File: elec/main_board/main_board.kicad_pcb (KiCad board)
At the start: 2 copper layers, 80 x 80 mm, 163 parts, among them J10 MJ-179PH, J13 B6B-ZR, J14 PinHeader, J15 PinHeader, J16 Fan motor, J2 Conn_01x22_Female, J3 PinHeader, J4 Conn_01x02, J5 Conn_01x02, J6 B6B-ZR, J7 EncSide, J8 B6B-ZR, J9 EncSide, Q1 DTC114E, Q10 IRLML6344, Q11 DMT6008LFG, Q12 DMT6008LFG, Q13 DMT6008LFG, Q14 MMBT3904, Q2 DTC114E, Q3 ST-1KL3A, Q4 ST-1KL3A, Q5 ST-1KL3A, Q6 ST-1KL3A, Q7 IRLML6344, Q8 IRLML6344, Q9 IRLML6344, SW1 TS-1088-AR02016, SW2 TS-1088-AR02016, SW3 TS-1088-AR02016, SW4 TS-1088-AR02016, SW5 TS-1088-AR02016, SW6 TS-1088-AR02016, U1 74LVC1G07SE-7, U10 LSM6DSR, U11 OKL-T/6-W12N-C, U12 XC6221B332MR, U13 LM74700QDBVRQ1, U14 MCP73213T-A6SI/MF, U15 LM74700QDBVRQ1, U16 FT231XQ-R, U17 FT231XQ-R, U18 SL2.1A, U19 INA219AIDCN, U2 ADCS7476, U20 ATmega328P-AU, U22 ESP32-S3-FN8, U3 ADCS7476, U4 BD63573NUV, U5 BD63573NUV, U6 ADCS7476, U7 ADCS7476, U8 AS5047D, U9 AS5047D, X1 CSTCE16M0V53-R0, X2 830108208709, Y2 X322512MSB4SI

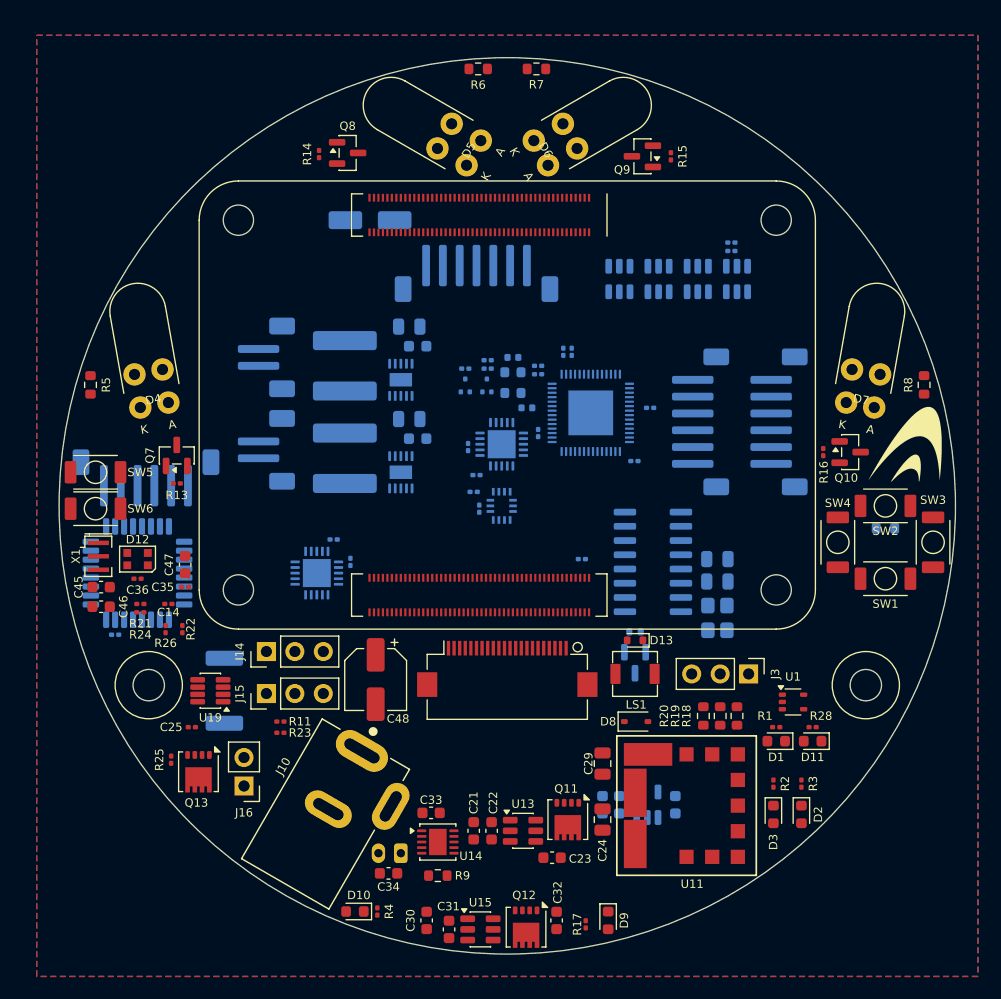
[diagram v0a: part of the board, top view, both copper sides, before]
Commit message: 配線作業中
Signed-off-by: Kazuki Iida <elkel53930@gmail.com>
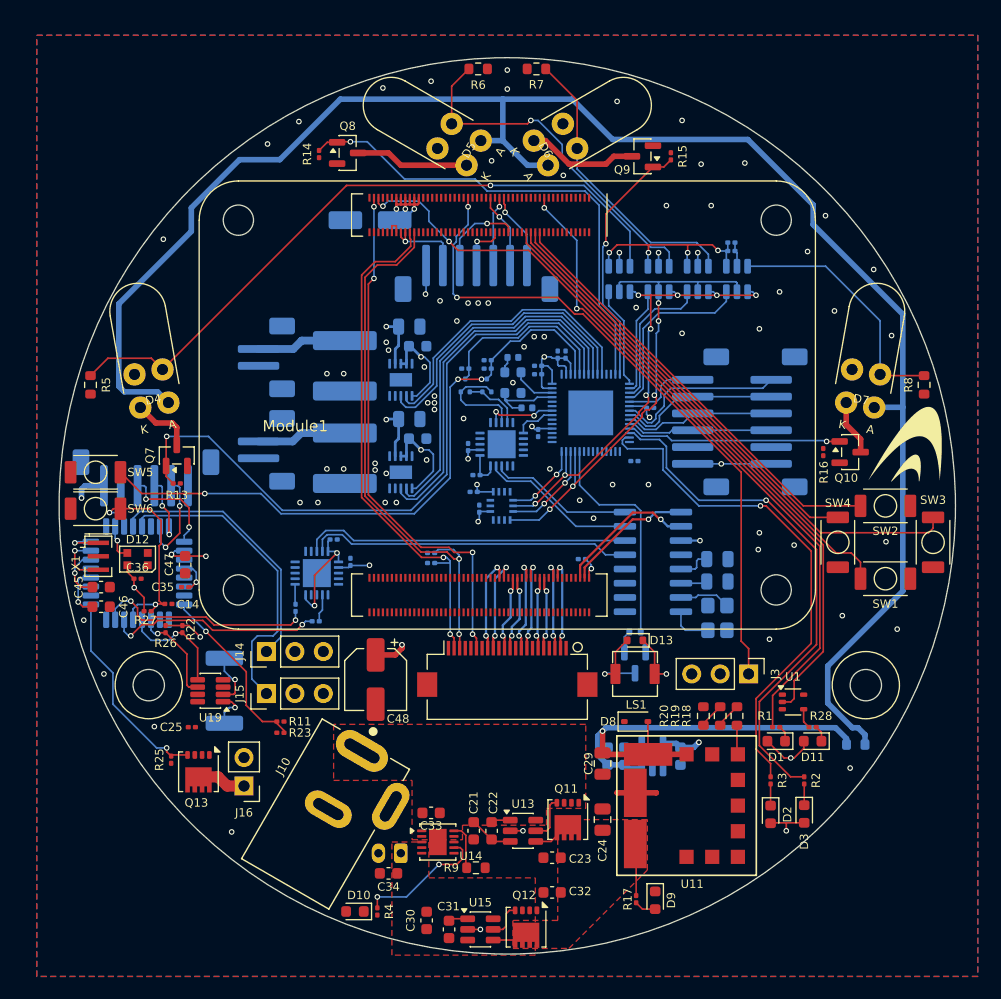
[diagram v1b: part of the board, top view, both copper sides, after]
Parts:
- added R32: RC0201FR-071KL, Resistor_SMD:R_0201_0603Metric, B.Cu at (138.2, 99.2)
- added R33: RC0201FR-071KL, Resistor_SMD:R_0201_0603Metric, B.Cu at (138.2, 100.1)
- R21, R24: moved to B.Cu
- R27: moved to F.Cu
- moved R12 19.5 mm to (176.1, 116.3)
- moved R24 15.7 mm to (127.9, 105.3), turned to 0 degrees
- moved R21 13.9 mm to (126.1, 104.1), turned to -90 degrees
- moved R17 5.03 mm to (156.5, 130.1)
- moved D9 4.57 mm to (158.2, 130.2)
- moved C26 4.36 mm to (153.9, 117.3)
- moved C27 4.36 mm to (155.4, 117.3)
- moved C28 4.36 mm to (160.4, 117.3)
- moved U12 4.36 mm to (157.9, 117.3)
- moved R27 3.58 mm to (112.9, 104.4)
- moved R9 3.47 mm to (142.2, 127.3), turned to 180 degrees
- moved R2 2.76 mm to (171.5, 119.5)
- moved R3 2.76 mm to (168.5, 119.5)
- moved D3 2.75 mm to (171.5, 122.5)
- moved D2 2.75 mm to (168.5, 122.5)
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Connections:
- C36 pad 1: GND -> +5V
- C36 pad 2: +5V -> GND
- J1 pad 2: /Compute Module/CM3V3 -> +3V3CM
- Module1 pad 24: unconnected-(Module1A-GPIO26-Pad24) -> /Compute Module/BTN_UP
- Module1 pad 26: unconnected-(Module1A-GPIO19-Pad26) -> /Compute Module/BTN_LEFT
- Module1 pad 28: unconnected-(Module1A-GPIO13-Pad28) -> /Compute Module/BTN_RIGHT
- Module1 pad 30: unconnected-(Module1A-GPIO6-Pad30) -> /Compute Module/BTN_DOWN
- Module1 pad 50: /Compute Module/BTN_RIGHT -> unconnected-(Module1A-GPIO17-Pad50)
- Module1 pad 54: /Compute Module/BTN_LEFT -> unconnected-(Module1A-GPIO4-Pad54)
- Module1 pad 56: /Compute Module/BTN_UP -> unconnected-(Module1A-GPIO3-Pad56)
- Module1 pad 58: /Compute Module/BTN_DOWN -> unconnected-(Module1A-GPIO2-Pad58)
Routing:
- net +3V3: track 0.00 -> 281.1 mm, vias 0 -> 16
- net +5V: track 0.00 -> 266.7 mm, vias 0 -> 15
- net Net-(D4-A): track 0.00 -> 156.2 mm
- net /Compute Module/nPWR_LED: track 0.00 -> 69.7 mm, vias 0 -> 2
- net Net-(Q3-E): track 0.00 -> 60.8 mm, vias 0 -> 1
- net /Micromouse/LF_EN: track 0.00 -> 60.4 mm, vias 0 -> 1
- net /Compute Module/FSV_SIG: track 0.00 -> 59.7 mm, vias 0 -> 2
- net Net-(Module1A-PI_nLED_Activity): track 0.00 -> 59.5 mm, vias 0 -> 2
- net /Micromouse/CHIP_PU: track 0.00 -> 57.3 mm, vias 0 -> 3
- net /Compute Module/BTN_RIGHT: track 0.00 -> 48.7 mm
- net /Compute Module/SCL0: track 0.00 -> 47.9 mm, vias 0 -> 2
- net /Micromouse/LED_1: track 0.00 -> 46.9 mm, vias 0 -> 1
- net /Compute Module/CAM_GPIO: track 0.00 -> 46.8 mm, vias 0 -> 4
- net /Compute Module/SDA0: track 0.00 -> 46.1 mm, vias 0 -> 2
- net /Micromouse/LED_0: track 0.00 -> 45.7 mm, vias 0 -> 1
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- added copper zone on F.Cu, net +BATT
- added copper zone on F.Cu, net /Power/EXT_PWR
- added copper zone on In1.Cu, net GND
- added copper zone on F.Cu, net Net-(BT1-+)
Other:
- copper layers 2 -> 4

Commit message: アートワーク完了
Signed-off-by: Kazuki Iida <elkel53930@gmail.com>
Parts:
- removed H1, H2, H3, H4: M2 mounting hole, MountingHole:MountingHole_2.2mm_M2
- removed J15: PinHeader, Connector_PinHeader_2.54mm:PinHeader_1x03_P2.54mm_Vertical
- removed U8, U9: AS5047D, Package_SO:TSSOP-14_4.4x5mm_P0.65mm
- added Q15: IRLML6344, Package_TO_SOT_SMD:SOT-23, B.Cu at (123.7, 108.8)
- added Q16: IRLML6344, Package_TO_SOT_SMD:SOT-23, B.Cu at (158.4, 68.0)
- added R34: 0603WAF1001T5E, Resistor_SMD:R_0603_1608Metric, B.Cu at (125.0, 113.6)
- added R35: RC0201FR-0710KL, Resistor_SMD:R_0201_0603Metric, B.Cu at (123.7, 106.5)
- added R36: 0603WAF1001T5E, Resistor_SMD:R_0603_1608Metric, B.Cu at (122.6, 112.4)
- added R37: RC0201FR-0710KL, Resistor_SMD:R_0201_0603Metric, B.Cu at (155.6, 67.8)
- C17: value CC0603KRX7R9BB104 -> CL10A475KO8NNNC; footprint Capacitor_SMD:C_0402_1005Metric -> Capacitor_SMD:C_0603_1608Metric; moved to B.Cu
- C18: value CL05B104KO5NNNC -> CL32A107MPVNNNE; footprint Capacitor_SMD:C_0402_1005Metric -> Capacitor_SMD:C_1210_3225Metric; moved to B.Cu
- C48: value RVT1A101M0505 -> CL32A107MPVNNNE; footprint Capacitor_SMD:CP_Elec_5x5.4 -> Capacitor_SMD:C_1210_3225Metric; moved to B.Cu
- C49: value RVT1A101M0505 -> CL32A107MPVNNNE; footprint Capacitor_SMD:CP_Elec_5x5.4 -> Capacitor_SMD:C_1210_3225Metric
- J7: value EncSide -> B4B-ZR; footprint Library:EncoderPad -> Connector_JST:JST_ZH_B4B-ZR_1x04_P1.50mm_Vertical
- J9: value EncSide -> B2B-ZR; footprint Library:EncoderPad -> Connector_JST:JST_ZH_B2B-ZR_1x02_P1.50mm_Vertical
- moved C17 181.1 mm to (137.4, 106.2), turned to 180 degrees
- moved J7 172.1 mm to (129.4, 111.0), turned to 180 degrees
- moved J9 164.3 mm to (165.2, 64.2), turned to 180 degrees
- moved C18 151.0 mm to (135.1, 70.9), turned to 90 degrees
- moved C49 50.5 mm to (124.7, 119.3), turned to 90 degrees
- moved R12 15.2 mm to (161.7, 121.0)
- moved J14 10.4 mm to (133.8, 107.9), turned to 0 degrees
- moved C48 6.12 mm to (132.8, 104.4)
- moved C25 6.08 mm to (119.1, 109.1)
- moved C26 1.56 mm to (153.9, 118.9), turned to 90 degrees
- moved C27 1.56 mm to (155.4, 118.9), turned to 90 degrees
- moved R23 1.00 mm to (124.1, 116.0), turned to 0 degrees
- moved R11 0.99 mm to (124.1, 115.0)
- moved SW5 0.99 mm to (109.1, 91.5)
- moved R6 0.90 mm to (142.4, 56.9)
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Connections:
- C17 pad 1: Net-(J7-Pin_2) -> +3V3CM
- C17 pad 2: Net-(J7-Pin_1) -> GND
- C18 pad 1: Net-(J9-Pin_2) -> GND
- C18 pad 2: Net-(J9-Pin_1) -> +5V
- C48 pad 1: +5V -> GND
- C48 pad 2: GND -> +5V
- C49 pad 1: +5V -> GND
- C49 pad 2: GND -> +BATT
- J7 pad 1: Net-(J7-Pin_1) -> +5V
- J7 pad 3: Net-(J7-Pin_3) -> +5V
- J7 pad 4: Net-(J7-Pin_4) -> /Arm/BD_AD
- J9 pad 1: Net-(J9-Pin_1) -> +BATT
- Module1 pad 25: unconnected-(Module1A-GPIO21-Pad25) -> /Compute Module/LIGHT
- U20 pad 13: /Arm/SERVO_SIG2 -> /Arm/BD_EN
- U20 pad 23: unconnected-(U20-PC0-Pad23) -> /Arm/BD_AD
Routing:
- net +3V3CM: track 7.22 -> 50.6 mm, vias 1 -> 6
- net /Arm/SERVO_SIG2: track 28.2 -> 0.00 mm
- net /Arm/BD_EN: track 0.00 -> 22.8 mm
- net +3V3: track 281.1 -> 298.6 mm, vias 16 -> 19
- net Net-(U17-~{DTR}): track 0.00 -> 15.9 mm, vias 0 -> 1
- net /Arm/BD_AD: track 0.00 -> 15.8 mm
- net /Power/EXT_PWR: track 3.98 -> 18.9 mm
- net /Compute Module/LIGHT: track 0.00 -> 11.7 mm, vias 0 -> 1
- net Net-(U16-3V3OUT): track 3.35 -> 11.6 mm, vias 0 -> 2
- net /Arm/SERVO_SIG1: track 24.2 -> 31.7 mm
- net GND: track 20.3 -> 27.8 mm, vias 77 -> 118
- net Net-(J9-Pin_2): track 0.00 -> 6.63 mm, vias 0 -> 1
- net +BATT: track 20.4 -> 24.5 mm, vias 2 -> 25
- net Net-(Q15-D): track 0.00 -> 4.03 mm
- net Net-(J7-Pin_2): track 0.00 -> 4.00 mm
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- added copper zone on B.Cu, net +5V
- added copper zone on B.Cu, net +BATT
- added copper zone on In2.Cu, net +BATT
- added copper zone on B.Cu, net Net-(J4-Pin_1)
- added copper zone on B.Cu, net Net-(J5-Pin_1)
- added copper zone on B.Cu, net Net-(U19-IN+)
- added copper zone on F.Cu, net Net-(U19-IN+)
- added copper zone on B.Cu, net Net-(U4-OUTB)
- added copper zone on B.Cu, net Net-(U5-OUTB)
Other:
- board text added: "- +"
- board text added: "AD 5V EN 5V"
- board text added: "CAMERA"
- board text added: "GND 5V S"
- board text added: "RPi-CM"
- board text added: "S 5V GND"
